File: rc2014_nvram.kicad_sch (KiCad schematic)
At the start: 13 parts, among them U1 CY62256-70PC, U2 74LS32, U3 CY62256-70PC, U6 74HCT04

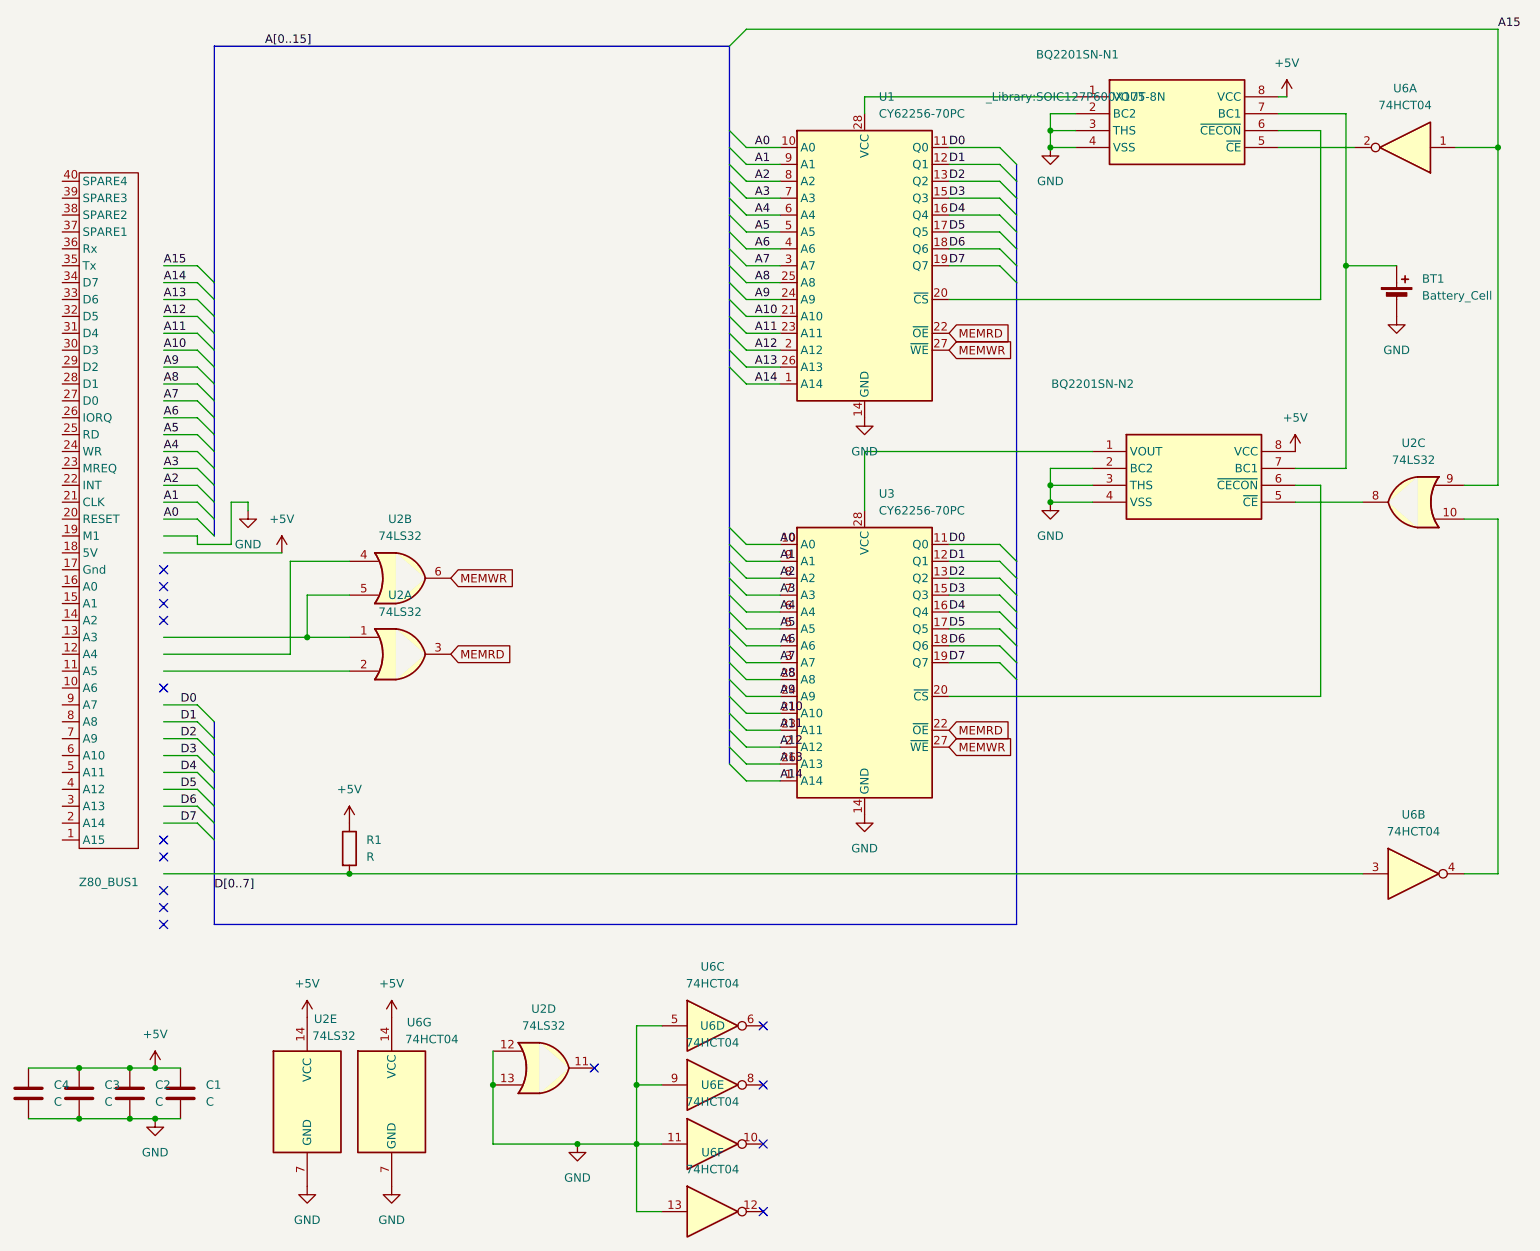
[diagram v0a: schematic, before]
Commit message: Fix grounding issues
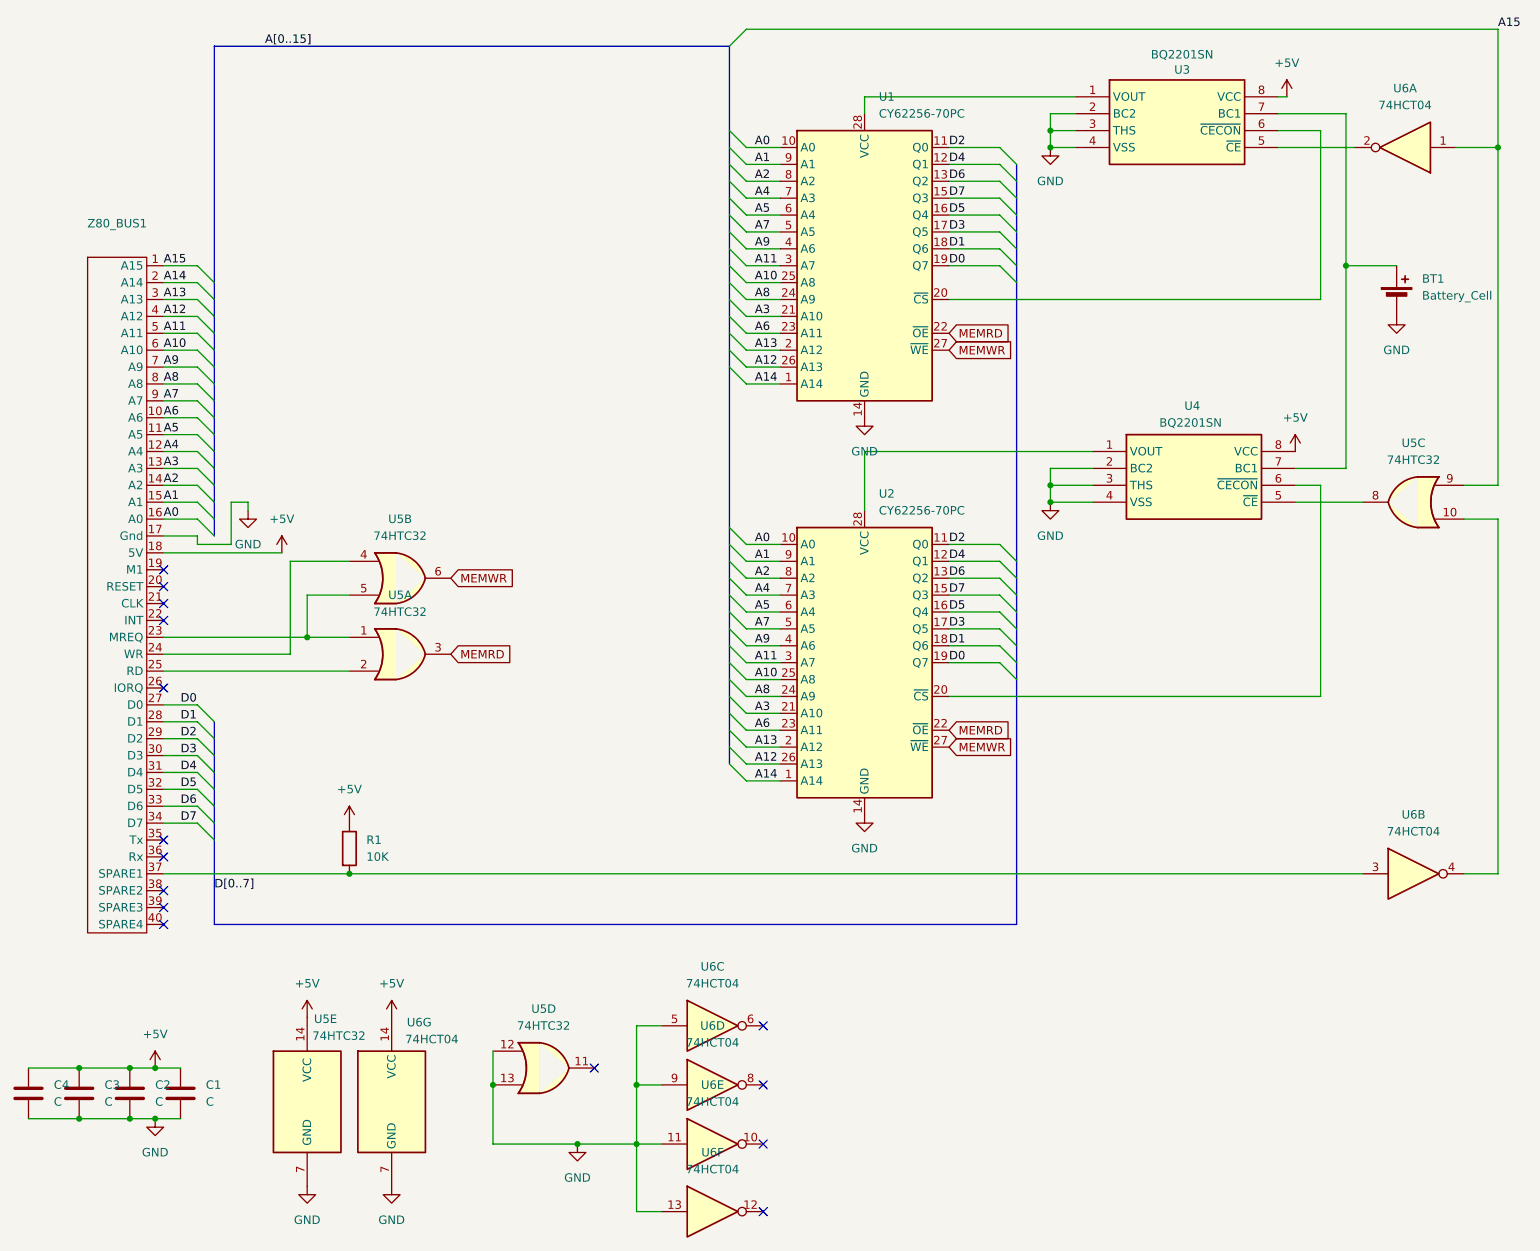
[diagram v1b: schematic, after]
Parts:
- R1: value R -> 10K
- U3: renamed from BQ2201SN-N1; value ~ -> BQ2201SN; footprint _Library:SOIC127P600X175-8N -> SOIC127P600X175-8N
- U4: renamed from BQ2201SN-N2; value ~ -> BQ2201SN; footprint _Library:SOIC127P600X175-8N -> SOIC127P600X175-8N
- U5: renamed from U2; value 74LS32 -> 74HTC32
- Z80_BUS1: footprint Connector_PinHeader_2.54mm:PinHeader_1x40_P2.54mm_Horizontal -> _Library:PinHeader_1x40_P2.54mm_Horizontal
- renumbered U3 to U2
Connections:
- net +5V: now also Z80_BUS1.18 (5V)
- net A0: now also Z80_BUS1.16 (A0)
- net A1: now also Z80_BUS1.15 (A1)
- net A10: now also U1.25 (A8), U2.25 (A8), Z80_BUS1.6 (A10); no longer U1.21 (A10), U2.21 (A10)
- net A11: now also U1.3 (A7), U2.3 (A7), Z80_BUS1.5 (A11); no longer U1.23 (A11), U2.23 (A11)
- net A12: now also U1.26 (A13), U2.26 (A13), Z80_BUS1.4 (A12); no longer U1.2 (A12), U2.2 (A12)
- net A13: now also U1.2 (A12), U2.2 (A12), Z80_BUS1.3 (A13); no longer U1.26 (A13), U2.26 (A13)
- net A14: now also Z80_BUS1.2 (A14)
- net A15: now also Z80_BUS1.1 (A15)
- net A2: now also Z80_BUS1.14 (A2)
- net A3: now also U1.21 (A10), U2.21 (A10), Z80_BUS1.13 (A3); no longer U1.7 (A3), U2.7 (A3)
- net A4: now also U1.7 (A3), U2.7 (A3), Z80_BUS1.12 (A4); no longer U1.6 (A4), U2.6 (A4)
- net A5: now also U1.6 (A4), U2.6 (A4), Z80_BUS1.11 (A5); no longer U1.5 (A5), U2.5 (A5)
- net A6: now also U1.23 (A11), U2.23 (A11), Z80_BUS1.10 (A6); no longer U1.4 (A6), U2.4 (A6)
- net A7: now also U1.5 (A5), U2.5 (A5), Z80_BUS1.9 (A7); no longer U1.3 (A7), U2.3 (A7)
- net A8: now also U1.24 (A9), U2.24 (A9), Z80_BUS1.8 (A8); no longer U1.25 (A8), U2.25 (A8)
- net A9: now also U1.4 (A6), U2.4 (A6), Z80_BUS1.7 (A9); no longer U1.24 (A9), U2.24 (A9)
- net D0: now also U1.19 (Q7), U2.19 (Q7), Z80_BUS1.27 (D0); no longer U1.11 (Q0), U2.11 (Q0)
- net D1: now also U1.18 (Q6), U2.18 (Q6), Z80_BUS1.28 (D1); no longer U1.12 (Q1), U2.12 (Q1)
- net D2: now also U1.11 (Q0), U2.11 (Q0), Z80_BUS1.29 (D2); no longer U1.13 (Q2), U2.13 (Q2)
- net D3: now also U1.17 (Q5), U2.17 (Q5), Z80_BUS1.30 (D3); no longer U1.15 (Q3), U2.15 (Q3)
- net D4: now also U1.12 (Q1), U2.12 (Q1), Z80_BUS1.31 (D4); no longer U1.16 (Q4), U2.16 (Q4)
- net D5: now also U1.16 (Q4), U2.16 (Q4), Z80_BUS1.32 (D5); no longer U1.17 (Q5), U2.17 (Q5)
- net D6: now also U1.13 (Q2), U2.13 (Q2), Z80_BUS1.33 (D6); no longer U1.18 (Q6), U2.18 (Q6)
- net D7: now also U1.15 (Q3), U2.15 (Q3), Z80_BUS1.34 (D7); no longer U1.19 (Q7), U2.19 (Q7)
- net GND: now also Z80_BUS1.17 (Gnd)
- net at Z80_BUS1.23 (MREQ): now also U5.1, U5.5
- net at Z80_BUS1.24 (WR): now also U5.4
- net at Z80_BUS1.25 (RD): now also U5.2
- net at Z80_BUS1.37 (SPARE1): now also R1.2, U6.3
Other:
- moved on the sheet: Z80_BUS1
